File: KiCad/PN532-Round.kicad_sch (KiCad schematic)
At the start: 52 parts, among them J1 Bell, J2 Bell, J3 0.1", SW1 ESE13V01D, U1 PN532, U2 QR, Y1 27.12MHz

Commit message: Library update
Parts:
- J3: value 0.1" -> TSM-104-02-L-SV; Manufacturer (none) -> Samtec; Note Non fit -> (none); PartNo (none) -> TSM-104-02-L-SV
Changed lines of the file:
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@@
     (in_bom yes) (on_board yes)
     (property "Reference" "J3" (id 0) (at 250.3932 71.6026 0))
-    (property "Value" "0.1\"" (id 1) (at 250.3932 73.914 0))
+    (property "Value" "TSM-104-02-L-SV" (id 1) (at 250.3932 73.914 0))
     (property "Footprint" "RevK:PinHeader_1x04_P2.54mm_Vertical_SMD_Pin1Right" (id 2) (at 247.65 78.74 0)
       (effects (font (size 1.27 1.27)) hide)
     )
-    (property "Datasheet" "~" (id 3) (at 247.65 78.74 0)
-      (effects (font (size 1.27 1.27)) hide)
-    )
-    (property "Note" "Non fit" (id 4) (at 247.65 78.74 0)
+    (property "Datasheet" "https://pdl.designspark.com/api/v1/manufacturers/98601efc6c674649abf42134/part/b4dcfc8d41594e97bc8aadd4/f3fea6d011fc4c3895b9a1d2/1.zip" (id 3) (at 247.65 78.74 0)
+      (effects (font (size 1.27 1.27)) hide)
+    )
+    (property "Note" "" (id 4) (at 247.65 78.74 0)
+      (effects (font (size 1.27 1.27)) hide)
+    )
+    (property "PartNo" "TSM-104-02-L-SV" (id 5) (at 247.65 78.74 0)
+      (effects (font (size 1.27 1.27)) hide)
+    )
+    (property "Manufacturer" "Samtec" (id 6) (at 247.65 78.74 0)
       (effects (font (size 1.27 1.27)) hide)
     )
@@
     )
     (path "/00000000-0000-0000-0000-0000607d486c"
-      (reference "J3") (unit 1) (value "0.1\"") (footprint "RevK:PinHeader_1x04_P2.54mm_Vertical_SMD_Pin1Right")
+      (reference "J3") (unit 1) (value "TSM-104-02-L-SV") (footprint "RevK:PinHeader_1x04_P2.54mm_Vertical_SMD_Pin1Right")
     )
     (path "/00000000-0000-0000-0000-0000609405db"

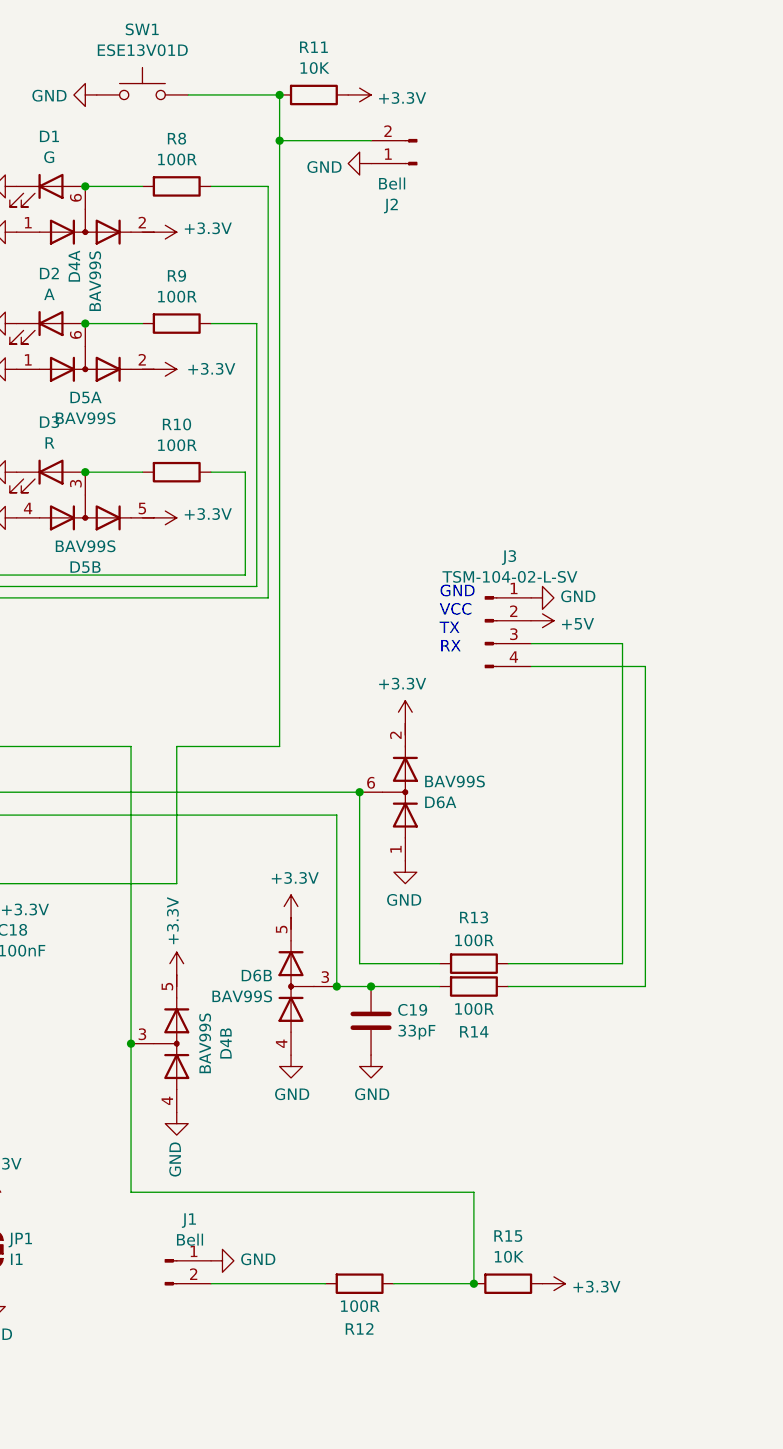
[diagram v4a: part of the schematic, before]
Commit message: Made bell part of connector, optional 4 or 5 way, and removed connector for tamper as not protected and good tamper switch now.
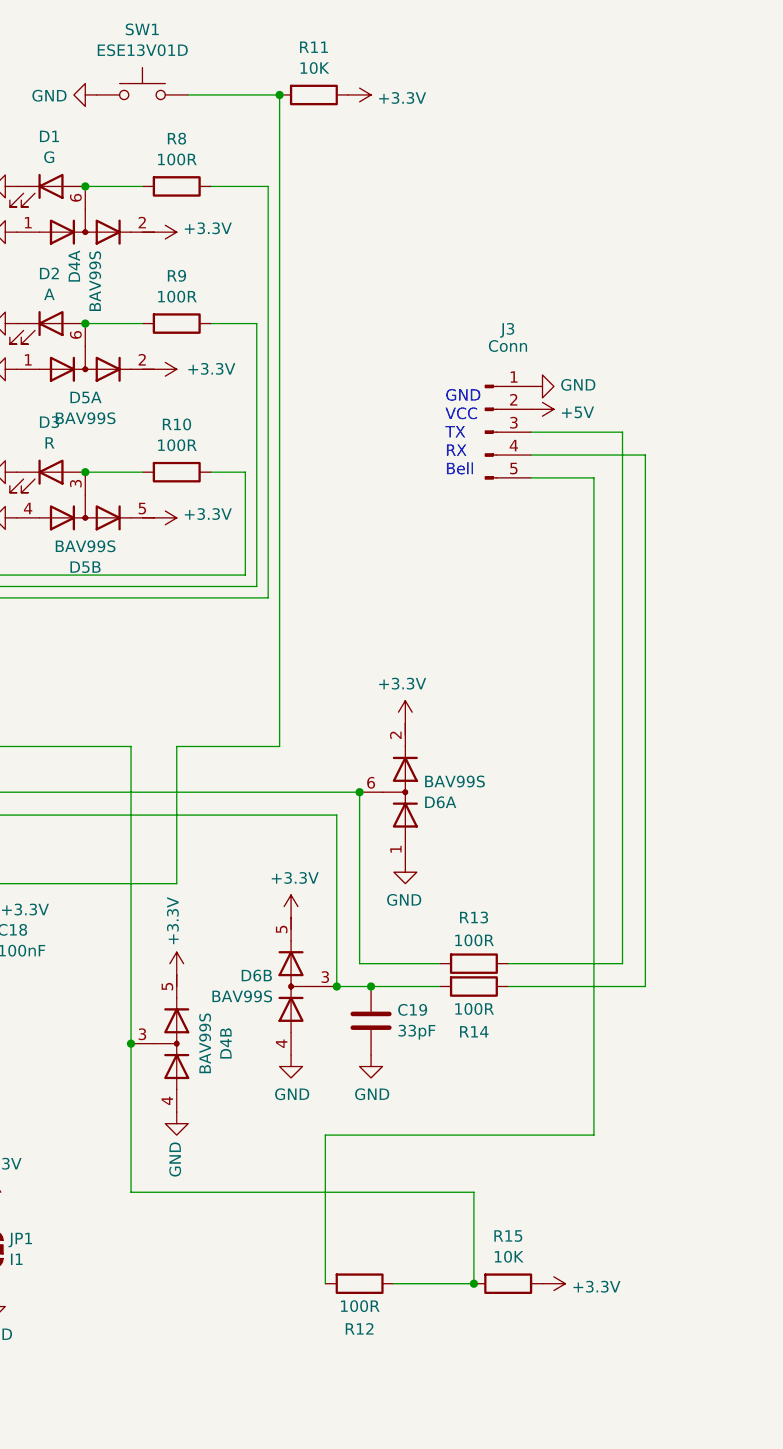
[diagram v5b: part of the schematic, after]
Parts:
- removed J1: Bell, RevK:PinHeader_1x02_P2.54mm_Vertical_SMD_Pin1Right, symbol Connector:Conn_01x02_Male
- removed J2: Bell, RevK:PinHeader_1x02_P2.54mm_Vertical_SMD_Pin1Left, symbol Connector:Conn_01x02_Male
- J3: value TSM-104-02-L-SV -> Conn; footprint RevK:PinHeader_1x04_P2.54mm_Vertical_SMD_Pin1Right -> RevK:PinHeader_1x05_P2.54mm_Vertical_SMD_Pin1Right; symbol Connector:Conn_01x04_Male -> Connector:Conn_01x05_Male; PartNo TSM-104-02-L-SV -> TSM-105-02-L-SV
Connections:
- net at R12.2: now also J3.5 (Pin_5)
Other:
- note added: "GND VCC TX RX Bell"
- note removed: "GND VCC TX RX"

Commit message: Revised connector
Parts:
- J3: footprint RevK:PinHeader_1x05_P2.54mm_Vertical_SMD_Pin1Right -> RevK:PinHeader_1x05_P2.54mm_Vertical_SMD_Pin1Left
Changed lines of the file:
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@@
     (property "Reference" "J3" (id 0) (at 250.19 46.355 0))
     (property "Value" "Conn" (id 1) (at 250.19 48.26 0))
-    (property "Footprint" "RevK:PinHeader_1x05_P2.54mm_Vertical_SMD_Pin1Right" (id 2) (at 247.65 57.785 0)
+    (property "Footprint" "RevK:PinHeader_1x05_P2.54mm_Vertical_SMD_Pin1Left" (id 2) (at 247.65 57.785 0)
       (effects (font (size 1.27 1.27)) hide)
     )
@@
     )
     (path "/00000000-0000-0000-0000-0000607d486c"
-      (reference "J3") (unit 1) (value "Conn") (footprint "RevK:PinHeader_1x05_P2.54mm_Vertical_SMD_Pin1Right")
+      (reference "J3") (unit 1) (value "Conn") (footprint "RevK:PinHeader_1x05_P2.54mm_Vertical_SMD_Pin1Left")
     )
     (path "/00000000-0000-0000-0000-0000609405db"
